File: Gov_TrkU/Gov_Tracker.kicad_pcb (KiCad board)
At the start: 2 copper layers, 75 x 91 mm, 168 parts, among them CN1 Main_Connector, J1 Conn_01x02, J10 Prog_T, J11 Debug, J2 USB_B_Mini, J3 USB_Con, J4 ANT, J5 Conn_Coaxial, J6 Debug/GPS_DBG, J7 Conn_Coaxial, J9 Prog_G, K2 G5Q-1, K3 SRA-05VDC-CL, Q1 SI2333DS, Q2 BC817, Q3 BC817, Q4 BSS84, Q5 BC817, U11 LM393, U12 W25Q128JVS, U13 STM32F103RCTx, U14 NEO-6M-GPS, U2 LM2596S-5, U3 SY7208B, U4 LM1117-3.3, U5 MCP73831-5-OT, U6 STM32F103RCTx, U7 693021020811, U8 SIM800C, U9 MAX3232, Y1 8MHz, Y4 32.678kHz, Y5 8MHz

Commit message: antenae swap
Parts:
- moved J7 27.4 mm to (160.8, 123.5), turned to 180 degrees
- moved R54 9.74 mm to (179.3, 122.6)
- moved L5 9.38 mm to (177.8, 127.2)
- moved J5 9.26 mm to (176.2, 132.3)
- moved J4 9.15 mm to (167.0, 132.2)
- moved U14 7.51 mm to (167.2, 118.0), turned to 180 degrees
- moved C13 3.28 mm to (153.0, 124.0)
- moved C38 1.85 mm to (158.0, 114.2)
- moved U8 1.46 mm to (172.8, 113.8), turned to 180 degrees
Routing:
- net +3V3: track 375.3 -> 407.4 mm, vias 9 -> 10
- net SIM_BAT: track 70.7 -> 100.2 mm, vias 4 -> 2
- net GND: track 1006.3 -> 1032.2 mm, vias 71 -> 81
- net Net-(U8-UART1_RXD): track 3.37 -> 25.4 mm
- net NW: track 5.09 -> 22.6 mm
- net ST: track 3.64 -> 21.2 mm
- net GPS_TX: track 73.2 -> 90.5 mm
- net GPS_RX: track 65.3 -> 82.4 mm
- net Net-(U8-UART1_TXD): track 7.63 -> 24.7 mm
- net GSM_PWR_RST: track 58.1 -> 74.6 mm, vias 2 -> 4
- net SIM_VDD: track 33.6 -> 20.9 mm
- net SIM_DATA: track 21.9 -> 26.7 mm
- net Net-(U14-VCC_RF): track 2.89 -> 6.18 mm
- net Net-(U8-VRTC): track 17.8 -> 15.0 mm
- net PRINTER_C_TX: track 38.0 -> 35.3 mm
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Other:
- board text added: "Gov_Trk 5.2.6 sim800"
- board text removed: "Gov_Trk 5.2.5 sim800"

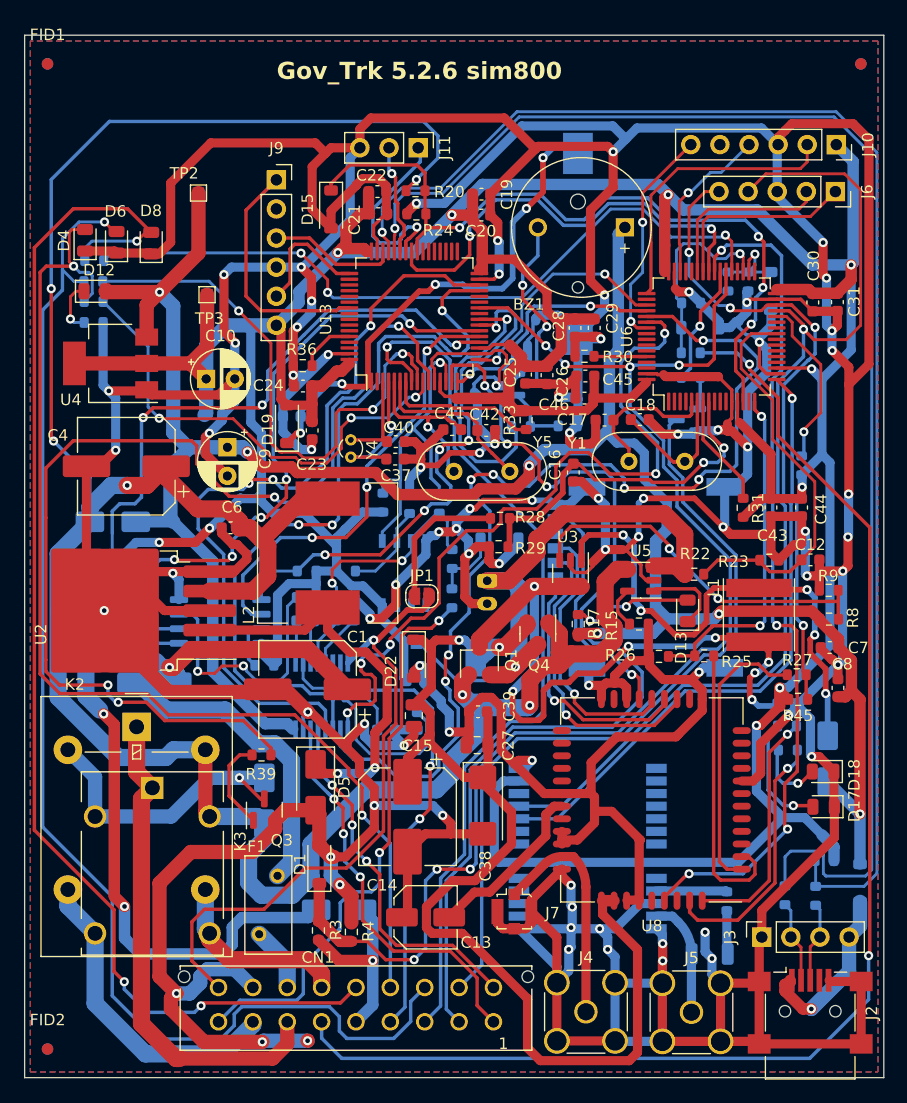
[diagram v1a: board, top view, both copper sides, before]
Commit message: updated the pannel and generated gerber files
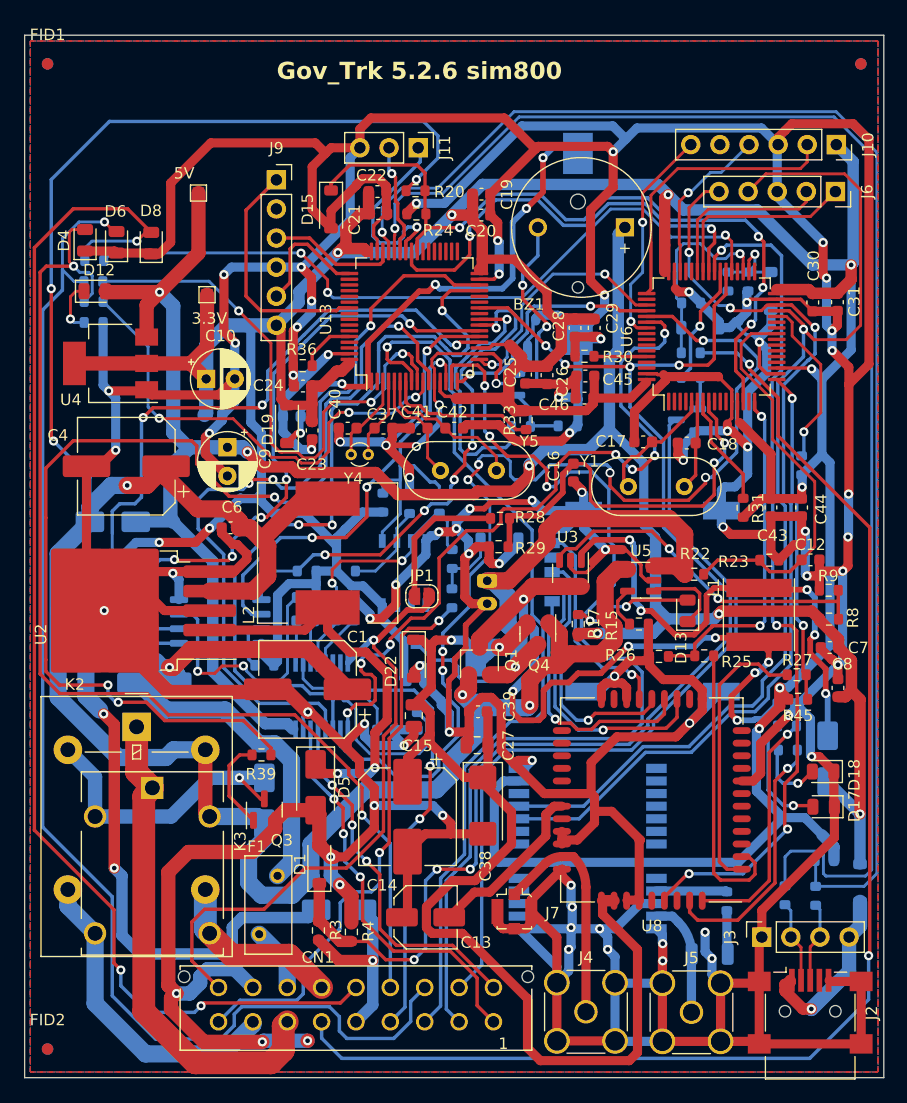
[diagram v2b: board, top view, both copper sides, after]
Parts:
- moved C18 4.58 mm to (175.8, 82.6), turned to 180 degrees
- moved C40 4.36 mm to (146.2, 81.3), turned to 180 degrees
- moved C17 3.87 mm to (172.0, 82.5)
- moved C41 2.93 mm to (152.4, 81.3)
- moved C37 2.89 mm to (149.3, 81.3)
- moved C42 2.81 mm to (155.5, 81.3)
- moved Y1 2.20 mm to (170.7, 86.4)
- moved U7 2.10 mm to (172.8, 96.4)
- moved Y4 1.54 mm to (148.0, 83.6), turned to 180 degrees
- moved Y5 1.18 mm to (154.3, 85.0)
- renumbered TP3 to 3.3V, TP2 to 5V
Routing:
- net GND: track 1032.2 -> 1039.1 mm
- net Net-(U13-PC15): track 12.2 -> 7.11 mm, vias 1 -> 0
- net FUEL_ADC: track 31.1 -> 36.1 mm
- net Net-(U13-PD0): track 15.0 -> 10.1 mm, vias 1 -> 0
- net /TRACKER/CR2: track 12.2 -> 7.90 mm
- net Net-(Q1-D): track 58.3 -> 61.8 mm
- net FUEL_TX: track 88.5 -> 91.9 mm
- net SIM_VDD: track 20.9 -> 18.0 mm
- net /TRACKER/CR1: track 12.9 -> 10.8 mm
- net Net-(U13-PD1): track 15.4 -> 13.5 mm
- net SIGNAL: track 29.0 -> 27.2 mm
- net FLASH_MOSI: track 47.7 -> 45.9 mm
- net +5V: track 198.6 -> 196.8 mm
- net PRNT_BTN: track 88.5 -> 90.1 mm
- net FUEL_RX: track 66.0 -> 64.5 mm, vias 5 -> 7
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
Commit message: updated the diode positioning
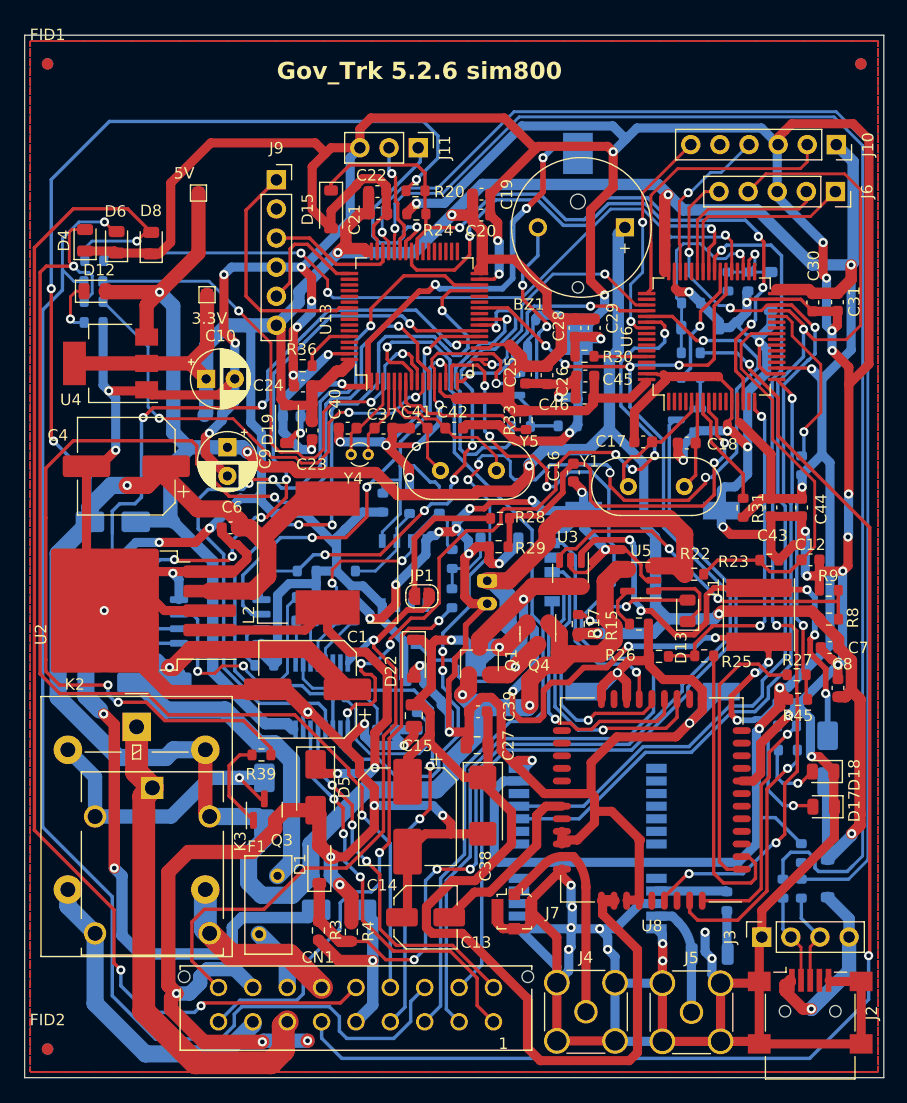
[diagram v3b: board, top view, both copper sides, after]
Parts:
- moved D14 2.85 mm to (188.1, 120.6)
- moved R21 2.13 mm to (185.8, 118.4), turned to -90 degrees
- moved R18 1.40 mm to (185.8, 121.5)
- moved R19 0.60 mm to (184.2, 121.5)
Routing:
- net +3V3: track 407.2 -> 403.4 mm
- net +5V: track 196.8 -> 200.4 mm
- net D-: track 125.1 -> 121.9 mm
- net D+: track 123.2 -> 121.6 mm
- net PRNT_BTN: track 90.1 -> 91.6 mm
- net D1+: track 7.06 -> 8.20 mm
- net VBS: track 18.8 -> 19.5 mm
- net D1-: track 7.18 -> 7.83 mm

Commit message: 5.2.6 final edit
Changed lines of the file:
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@@
     (property "ki_keywords" "fiducial marker")
     (attr smd)
-    (fp_text reference "FID2" (at 0 -2.54) (layer "F.SilkS")
+    (fp_text reference "FID2" (at 0 -2.54) (layer "F.SilkS") hide
         (effects (font (size 1 1) (thickness 0.15)))
     )
@@
     (property "ki_keywords" "fiducial marker")
     (attr smd)
-    (fp_text reference "FID1" (at 0 -2.54) (layer "F.SilkS")
+    (fp_text reference "FID1" (at 0 -2.54) (layer "F.SilkS") hide
         (effects (font (size 1 1) (thickness 0.15)))
     )
@@
     (property "ki_keywords" "fiducial marker")
     (attr smd)
-    (fp_text reference "FID6" (at 0 2) (layer "B.SilkS")
+    (fp_text reference "FID6" (at 0 2) (layer "B.SilkS") hide
         (effects (font (size 1 1) (thickness 0.15)) (justify mirror))
     )
@@
     (property "ki_keywords" "fiducial marker")
     (attr smd)
-    (fp_text reference "FID5" (at 0 2) (layer "B.SilkS")
+    (fp_text reference "FID5" (at 0 2) (layer "B.SilkS") hide
         (effects (font (size 1 1) (thickness 0.15)) (justify mirror))
     )
@@
     )
   )
-  (group "" (id 72b0f4be-18a9-4842-9496-1feffa67924e)
+  (group "" (id 95bcc70e-c661-41f2-941c-6a83b5ddd0ba)
     (members
       0008ad96-9d2c-4335-9a1c-9a74e0a4724c
